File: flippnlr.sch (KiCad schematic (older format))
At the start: 87 parts, among them J1 Pwr In, J2 TP3, J3 TP1, J4 Opt Out, J5 Opt Out, J6 Data Out, J7 Data In, J8 TP2, U1 LD1117 3.3V, U10 TPL7407LA, U11 TPL7407LA, U12 TPL7407LA, U13 SN74HCS365, U2 SN74HCS594, U3 SN74HCS594, U4 SN74HCS594, U5 SN74HCS594, U6 SN74HCS594, U7 TPL7407LA, U8 TPL7407LA, U9 TPL7407LA

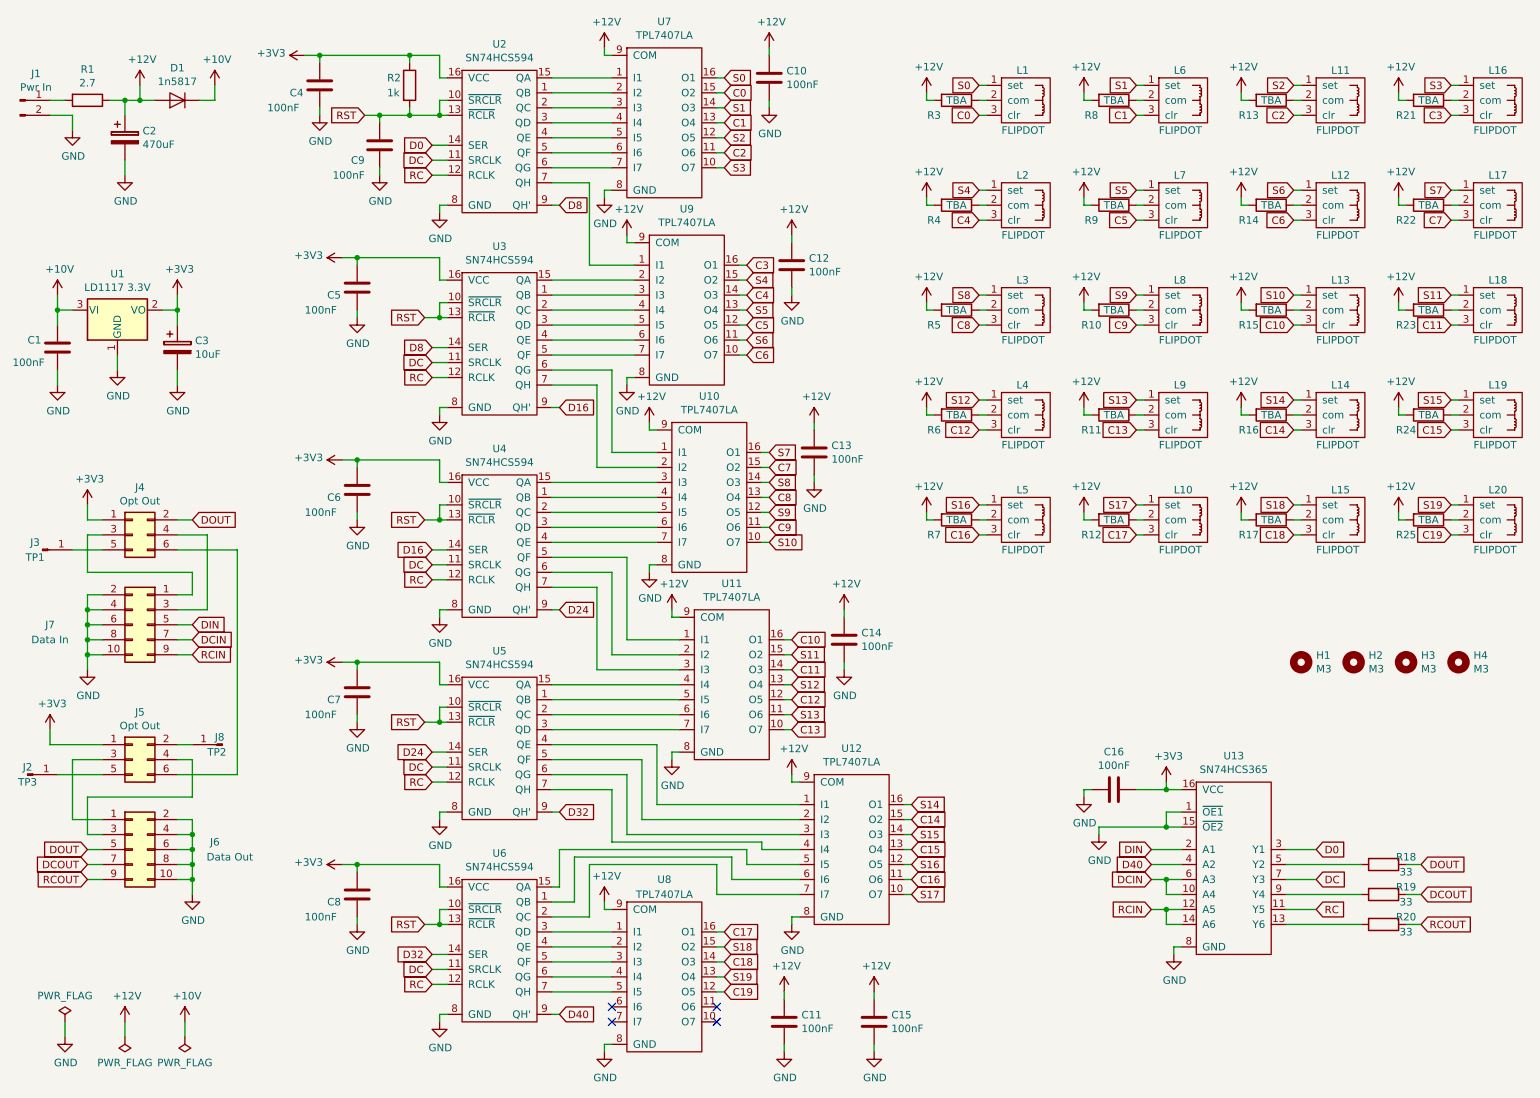
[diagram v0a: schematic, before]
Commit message: fix kicad lib path and begin layout
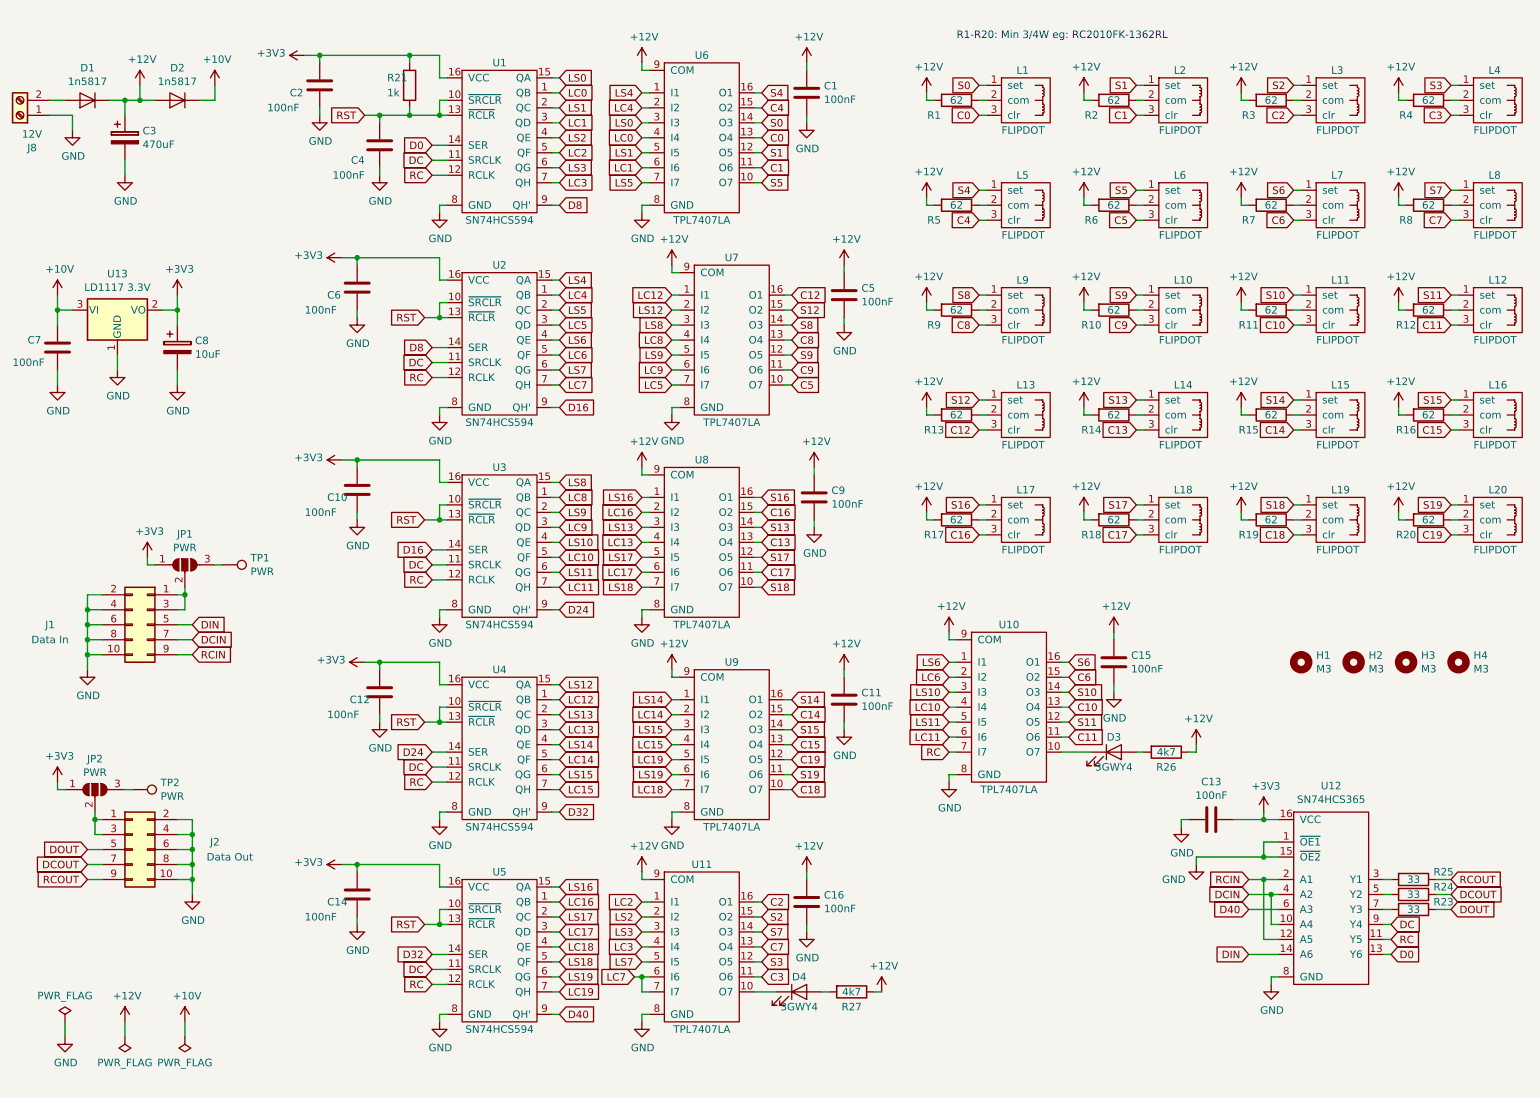
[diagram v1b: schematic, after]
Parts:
- removed J1: Pwr In, Connector_PinHeader_2.54mm:PinHeader_2x01_P2.54mm_Vertical, symbol Connector:Conn_01x02_Male
- removed J2: TP3, Connector_PinHeader_2.54mm:PinHeader_1x01_P2.54mm_Vertical, symbol Connector:Conn_01x01_Male
- removed J3: TP1, Connector_PinHeader_2.54mm:PinHeader_1x01_P2.54mm_Vertical, symbol Connector:Conn_01x01_Male
- removed J4, J5: Opt Out, Connector_PinHeader_2.54mm:PinHeader_2x03_P2.54mm_Vertical, symbol Connector_Generic:Conn_02x03_Odd_Even
- removed J8: TP2, Connector_PinHeader_2.54mm:PinHeader_1x01_P2.54mm_Vertical, symbol Connector:Conn_01x01_Male
- removed R1: 2.7, Resistor_THT:R_Axial_DIN0309_L9.0mm_D3.2mm_P12.70mm_Horizontal, symbol Device:R
- added D1: 1n5817, Diode_THT:D_A-405_P10.16mm_Horizontal, symbol Device:D
- added D3, D4: 3GWY4, LED_THT:LED_D3.0mm, symbol Device:LED
- added J8: 12V, TerminalBlock_Phoenix:TerminalBlock_Phoenix_PT-1,5-2-5.0-H_1x02_P5.00mm_Horizontal, symbol Connector:Screw_Terminal_01x02
- added JP1, JP2: PWR, Jumper:SolderJumper-3_P1.3mm_Open_RoundedPad1.0x1.5mm, symbol Jumper:SolderJumper_3_Open
- added R26, R27: 4k7, Resistor_SMD:R_0805_2012Metric_Pad1.15x1.40mm_HandSolder, symbol Device:R
- added TP1, TP2: PWR, TestPoint:TestPoint_Pad_D2.0mm, symbol Connector:TestPoint
- L1, L20: footprint Connector_PinHeader_2.54mm:PinHeader_1x03_P2.54mm_Vertical -> flipdot:Flipdot
- L10: renamed from L8; footprint Connector_PinHeader_2.54mm:PinHeader_1x03_P2.54mm_Vertical -> flipdot:Flipdot
- L11: renamed from L13; footprint Connector_PinHeader_2.54mm:PinHeader_1x03_P2.54mm_Vertical -> flipdot:Flipdot
- L12: renamed from L18; footprint Connector_PinHeader_2.54mm:PinHeader_1x03_P2.54mm_Vertical -> flipdot:Flipdot
- L13: renamed from L4; footprint Connector_PinHeader_2.54mm:PinHeader_1x03_P2.54mm_Vertical -> flipdot:Flipdot
- L14: renamed from L9; footprint Connector_PinHeader_2.54mm:PinHeader_1x03_P2.54mm_Vertical -> flipdot:Flipdot
- L15: renamed from L14; footprint Connector_PinHeader_2.54mm:PinHeader_1x03_P2.54mm_Vertical -> flipdot:Flipdot
- L16: renamed from L19; footprint Connector_PinHeader_2.54mm:PinHeader_1x03_P2.54mm_Vertical -> flipdot:Flipdot
- L17: renamed from L5; footprint Connector_PinHeader_2.54mm:PinHeader_1x03_P2.54mm_Vertical -> flipdot:Flipdot
- L18: renamed from L10; footprint Connector_PinHeader_2.54mm:PinHeader_1x03_P2.54mm_Vertical -> flipdot:Flipdot
- L19: renamed from L15; footprint Connector_PinHeader_2.54mm:PinHeader_1x03_P2.54mm_Vertical -> flipdot:Flipdot
- L2: renamed from L6; footprint Connector_PinHeader_2.54mm:PinHeader_1x03_P2.54mm_Vertical -> flipdot:Flipdot
- L3: renamed from L11; footprint Connector_PinHeader_2.54mm:PinHeader_1x03_P2.54mm_Vertical -> flipdot:Flipdot
- L4: renamed from L16; footprint Connector_PinHeader_2.54mm:PinHeader_1x03_P2.54mm_Vertical -> flipdot:Flipdot
- L5: renamed from L2; footprint Connector_PinHeader_2.54mm:PinHeader_1x03_P2.54mm_Vertical -> flipdot:Flipdot
- L6: renamed from L7; footprint Connector_PinHeader_2.54mm:PinHeader_1x03_P2.54mm_Vertical -> flipdot:Flipdot
- L7: renamed from L12; footprint Connector_PinHeader_2.54mm:PinHeader_1x03_P2.54mm_Vertical -> flipdot:Flipdot
- L8: renamed from L17; footprint Connector_PinHeader_2.54mm:PinHeader_1x03_P2.54mm_Vertical -> flipdot:Flipdot
- L9: renamed from L3; footprint Connector_PinHeader_2.54mm:PinHeader_1x03_P2.54mm_Vertical -> flipdot:Flipdot
- R1: renamed from R3; value TBA -> 62; footprint Resistor_SMD:R_1210_3225Metric_Pad1.42x2.65mm_HandSolder -> Resistor_SMD:R_2010_5025Metric_Pad1.52x2.65mm_HandSolder
- R10: value TBA -> 62; footprint Resistor_SMD:R_1210_3225Metric_Pad1.42x2.65mm_HandSolder -> Resistor_SMD:R_2010_5025Metric_Pad1.52x2.65mm_HandSolder
- R11: renamed from R15; value TBA -> 62; footprint Resistor_SMD:R_1210_3225Metric_Pad1.42x2.65mm_HandSolder -> Resistor_SMD:R_2010_5025Metric_Pad1.52x2.65mm_HandSolder
- R12: renamed from R23; value TBA -> 62; footprint Resistor_SMD:R_1210_3225Metric_Pad1.42x2.65mm_HandSolder -> Resistor_SMD:R_2010_5025Metric_Pad1.52x2.65mm_HandSolder
- R13: renamed from R6; value TBA -> 62; footprint Resistor_SMD:R_1210_3225Metric_Pad1.42x2.65mm_HandSolder -> Resistor_SMD:R_2010_5025Metric_Pad1.52x2.65mm_HandSolder
- R14: renamed from R11; value TBA -> 62; footprint Resistor_SMD:R_1210_3225Metric_Pad1.42x2.65mm_HandSolder -> Resistor_SMD:R_2010_5025Metric_Pad1.52x2.65mm_HandSolder
- R15: renamed from R16; value TBA -> 62; footprint Resistor_SMD:R_1210_3225Metric_Pad1.42x2.65mm_HandSolder -> Resistor_SMD:R_2010_5025Metric_Pad1.52x2.65mm_HandSolder
- R16: renamed from R24; value TBA -> 62; footprint Resistor_SMD:R_1210_3225Metric_Pad1.42x2.65mm_HandSolder -> Resistor_SMD:R_2010_5025Metric_Pad1.52x2.65mm_HandSolder
- R17: renamed from R7; value TBA -> 62; footprint Resistor_SMD:R_1210_3225Metric_Pad1.42x2.65mm_HandSolder -> Resistor_SMD:R_2010_5025Metric_Pad1.52x2.65mm_HandSolder
- R18: renamed from R12; value TBA -> 62; footprint Resistor_SMD:R_1210_3225Metric_Pad1.42x2.65mm_HandSolder -> Resistor_SMD:R_2010_5025Metric_Pad1.52x2.65mm_HandSolder
- R19: renamed from R17; value TBA -> 62; footprint Resistor_SMD:R_1210_3225Metric_Pad1.42x2.65mm_HandSolder -> Resistor_SMD:R_2010_5025Metric_Pad1.52x2.65mm_HandSolder
- R2: renamed from R8; value TBA -> 62; footprint Resistor_SMD:R_1210_3225Metric_Pad1.42x2.65mm_HandSolder -> Resistor_SMD:R_2010_5025Metric_Pad1.52x2.65mm_HandSolder
- R20: renamed from R25; value TBA -> 62; footprint Resistor_SMD:R_1210_3225Metric_Pad1.42x2.65mm_HandSolder -> Resistor_SMD:R_2010_5025Metric_Pad1.52x2.65mm_HandSolder
- R3: renamed from R13; value TBA -> 62; footprint Resistor_SMD:R_1210_3225Metric_Pad1.42x2.65mm_HandSolder -> Resistor_SMD:R_2010_5025Metric_Pad1.52x2.65mm_HandSolder
- R4: renamed from R21; value TBA -> 62; footprint Resistor_SMD:R_1210_3225Metric_Pad1.42x2.65mm_HandSolder -> Resistor_SMD:R_2010_5025Metric_Pad1.52x2.65mm_HandSolder
- R5: renamed from R4; value TBA -> 62; footprint Resistor_SMD:R_1210_3225Metric_Pad1.42x2.65mm_HandSolder -> Resistor_SMD:R_2010_5025Metric_Pad1.52x2.65mm_HandSolder
- R6: renamed from R9; value TBA -> 62; footprint Resistor_SMD:R_1210_3225Metric_Pad1.42x2.65mm_HandSolder -> Resistor_SMD:R_2010_5025Metric_Pad1.52x2.65mm_HandSolder
- R7: renamed from R14; value TBA -> 62; footprint Resistor_SMD:R_1210_3225Metric_Pad1.42x2.65mm_HandSolder -> Resistor_SMD:R_2010_5025Metric_Pad1.52x2.65mm_HandSolder
- R8: renamed from R22; value TBA -> 62; footprint Resistor_SMD:R_1210_3225Metric_Pad1.42x2.65mm_HandSolder -> Resistor_SMD:R_2010_5025Metric_Pad1.52x2.65mm_HandSolder
- R9: renamed from R5; value TBA -> 62; footprint Resistor_SMD:R_1210_3225Metric_Pad1.42x2.65mm_HandSolder -> Resistor_SMD:R_2010_5025Metric_Pad1.52x2.65mm_HandSolder
- renumbered C10 to C1, C6 to C10, C14 to C11, C7 to C12, C16 to C13, C8 to C14, C11 to C15, C15 to C16, C4 to C2, C2 to C3, C9 to C4, C12 to C5, C5 to C6, C1 to C7, C3 to C8, C13 to C9, D1 to D2, J7 to J1, J6 to J2, R2 to R21, R18 to R23, R19 to R24, R20 to R25, U2 to U1, U12 to U10, U8 to U11, U13 to U12, U1 to U13, U3 to U2, U4 to U3, U5 to U4, U6 to U5, U7 to U6, U9 to U7, U10 to U8, U11 to U9
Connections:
- net +12V: now also D1.1 (K), R26.1, R27.1
- net +3V3: now also JP1.1 (A), JP2.1 (A)
- net C0: now also U6.13 (O4); no longer U6.15 (O2)
- net C1: now also U6.11 (O6); no longer U6.13 (O4)
- net C10: now also U10.13 (O4); no longer U9.16 (O1)
- net C11: now also U10.11 (O6); no longer U9.14 (O3)
- net C12: now also U7.16 (O1); no longer U9.12 (O5)
- net C13: now also U8.13 (O4); no longer U9.10 (O7)
- net C14: now also U9.15 (O2); no longer U10.15 (O2)
- net C15: now also U9.13 (O4); no longer U10.13 (O4)
- net C16: now also U8.15 (O2); no longer U10.11 (O6)
- net C17: now also U8.11 (O6); no longer U11.16 (O1)
- net C18: now also U9.10 (O7); no longer U11.14 (O3)
- net C19: now also U9.12 (O5); no longer U11.12 (O5)
- net C2: now also U11.16 (O1); no longer U6.11 (O6)
- net C3: now also U11.11 (O6); no longer U7.16 (O1)
- net C4: now also U6.15 (O2); no longer U7.14 (O3)
- net C5: now also U7.10 (O7); no longer U7.12 (O5)
- net C6: now also U10.15 (O2); no longer U7.10 (O7)
- net C7: now also U11.13 (O4); no longer U8.15 (O2)
- net C8: now also U7.13 (O4); no longer U8.13 (O4)
- net C9: now also U7.11 (O6); no longer U8.11 (O6)
- net D0: now also U12.13 (Y6); no longer U12.3 (Y1)
- net D40: now also U12.6 (A3); no longer U12.4 (A2)
- net DC: now also U12.9 (Y4); no longer U12.7 (Y3)
- net DCIN: now also U12.4 (A2); no longer U12.6 (A3)
- net DIN: now also U12.14 (A6); no longer U12.2 (A1)
- net GND: now also J8.1 (Pin_1)
- net RC: now also U10.7 (I7)
- net RCIN: now also U12.2 (A1); no longer U12.14 (A6)
- net S0: now also U6.14 (O3); no longer U6.16 (O1)
- net S1: now also U6.12 (O5); no longer U6.14 (O3)
- net S10: now also U10.14 (O3); no longer U8.10 (O7)
- net S11: now also U10.12 (O5); no longer U9.15 (O2)
- net S12: now also U7.15 (O2); no longer U9.13 (O4)
- net S13: now also U8.14 (O3); no longer U9.11 (O6)
- net S14: now also U9.16 (O1); no longer U10.16 (O1)
- net S15: now also U9.14 (O3); no longer U10.14 (O3)
- net S16: now also U8.16 (O1); no longer U10.12 (O5)
- net S17: now also U8.12 (O5); no longer U10.10 (O7)
- net S18: now also U8.10 (O7); no longer U11.15 (O2)
- net S19: now also U9.11 (O6); no longer U11.13 (O4)
- net S2: now also U11.15 (O2); no longer U6.12 (O5)
- net S3: now also U11.12 (O5); no longer U6.10 (O7)
- net S4: now also U6.16 (O1); no longer U7.15 (O2)
- net S5: now also U6.10 (O7); no longer U7.13 (O4)
- net S6: now also U10.16 (O1); no longer U7.11 (O6)
- net S7: now also U11.14 (O3); no longer U8.16 (O1)
- net S8: now also U7.14 (O3); no longer U8.14 (O3)
- net S9: now also U7.12 (O5); no longer U8.12 (O5)
- net at J1.1 (Pin_1): now also J1.3 (Pin_3), JP1.2 (C)
- net at J2.1 (Pin_1): now also J2.3 (Pin_3), JP2.2 (C)
- net at R25.2: now also U12.3 (Y1); no longer U12.13 (Y6)
- net at R24.2: now also U12.5 (Y2); no longer U12.9 (Y4)
- net at R23.2: now also U12.7 (Y3); no longer U12.5 (Y2)
- net LC17: now reaches U5.3 (QD)
- net LC17: now also U8.6 (I6); no longer U11.1 (I1)
- net at U11.10 (O7): now also D4.1 (K)
- net LC18: now reaches U5.4 (QE)
- net LC18: now also U9.7 (I7); no longer U11.2 (I2)
- net LS18: now reaches U5.5 (QF)
- net LS18: now also U8.7 (I7); no longer U11.3 (I3)
- net LC3: now reaches U11.4 (I4)
- net LC3: now also U1.7 (QH); no longer U5.6 (QG)
- net LC19: now reaches U5.7 (QH)
- net LC19: now also U9.5 (I5); no longer U11.5 (I5)
- net LC7: now reaches U11.6 (I6)
- net LC7: now also U11.7 (I7), U2.7 (QH)
- net LC0: now reaches U1.1 (QB)
- net LC0: now also U6.4 (I4); no longer U6.2 (I2)
- net LS0: now reaches U1.15 (QA)
- net LS0: now also U6.3 (I3); no longer U6.1 (I1)
- net LS1: now reaches U1.2 (QC)
- net LS1: now also U6.5 (I5); no longer U6.3 (I3)
- net LC1: now reaches U1.3 (QD)
- net LC1: now also U6.6 (I6); no longer U6.4 (I4)
- net LS2: now reaches U1.4 (QE)
- net LS2: now also U11.2 (I2); no longer U6.5 (I5)
- net LC2: now reaches U1.5 (QF)
- net LC2: now also U11.1 (I1); no longer U6.6 (I6)
- net LS3: now reaches U1.6 (QG)
- net LS3: now also U11.3 (I3); no longer U6.7 (I7)
- net LC12: now reaches U7.1 (I1)
- net LC12: now also U4.1 (QB); no longer U1.7 (QH)
- net LC10: now reaches U3.5 (QF)
- net LC10: now also U10.4 (I4); no longer U9.1 (I1)
- net LC14: now reaches U9.2 (I2)
- net LC14: now also U4.5 (QF); no longer U3.6 (QG)
- net LC11: now reaches U3.7 (QH)
- net LC11: now also U10.6 (I6); no longer U9.3 (I3)
- net LC15: now reaches U9.4 (I4)
- net LC15: now also U4.7 (QH); no longer U4.15 (QA)
- net LS13: now reaches U4.2 (QC)
- net LS13: now also U8.3 (I3); no longer U9.6 (I6)
- net LC13: now reaches U4.3 (QD)
- net LC13: now also U8.4 (I4); no longer U9.7 (I7)
- net LC4: now reaches U2.1 (QB)
- net LC4: now also U6.2 (I2); no longer U7.3 (I3)
- net LS12: now reaches U7.2 (I2)
- net LS12: now also U4.15 (QA); no longer U2.15 (QA)
- net LC8: now reaches U7.4 (I4)
- net LC8: now also U3.1 (QB); no longer U2.2 (QC)
- net LC5: now reaches U2.3 (QD)
- net LC5: now also U7.7 (I7); no longer U7.5 (I5)
- net LC9: now reaches U7.6 (I6)
- net LC9: now also U3.3 (QD); no longer U2.4 (QE)
- net LC6: now reaches U2.5 (QF)
- net LC6: now also U10.2 (I2); no longer U7.7 (I7)
- net LS16: now reaches U8.1 (I1)
- net LS16: now also U5.15 (QA); no longer U2.6 (QG)
- net LC16: now reaches U8.2 (I2)
- net LC16: now also U5.1 (QB); no longer U2.7 (QH)
- net LS14: now reaches U4.4 (QE)
- net LS14: now also U9.1 (I1); no longer U10.1 (I1)
- net LS10: now reaches U10.3 (I3)
- net LS10: now also U3.4 (QE); no longer U4.6 (QG)
- net LS11: now reaches U10.5 (I5)
- net LS11: now also U3.6 (QG); no longer U5.15 (QA)
- net LS17: now reaches U5.2 (QC)
- net LS17: now also U8.5 (I5); no longer U10.7 (I7)
- net LS8: now reaches U3.15 (QA)
- net LS8: now also U7.3 (I3); no longer U8.3 (I3)
- net LS9: now reaches U3.2 (QC)
- net LS9: now also U7.5 (I5); no longer U8.5 (I5)
- new net: D3.1 (K), U10.10 (O7)
- new net: D3.2 (A), R26.2
- new net: D4.2 (A), R27.2
- new net: JP1.3 (B), TP1.1
- new net: JP2.3 (B), TP2.1
- new net: D1.2 (A), J8.2 (Pin_2)
- new net LS15: U4.6 (QG), U9.3 (I3)
- new net LS19: U5.6 (QG), U9.6 (I6)
- new net LS4: U2.15 (QA), U6.1 (I1)
- new net LS5: U2.2 (QC), U6.7 (I7)
- new net LS6: U10.1 (I1), U2.4 (QE)
- new net LS7: U11.5 (I5), U2.6 (QG)
- no-connect marks 4 -> 0
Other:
- note added: "R1-R20: Min 3/4W eg: RC2010FK-1362RL"
- moved on the sheet: C1, C11, C12, C13, C15, C16, C5, C9, R23, R24, R25, U10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

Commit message: reroute signals slightly
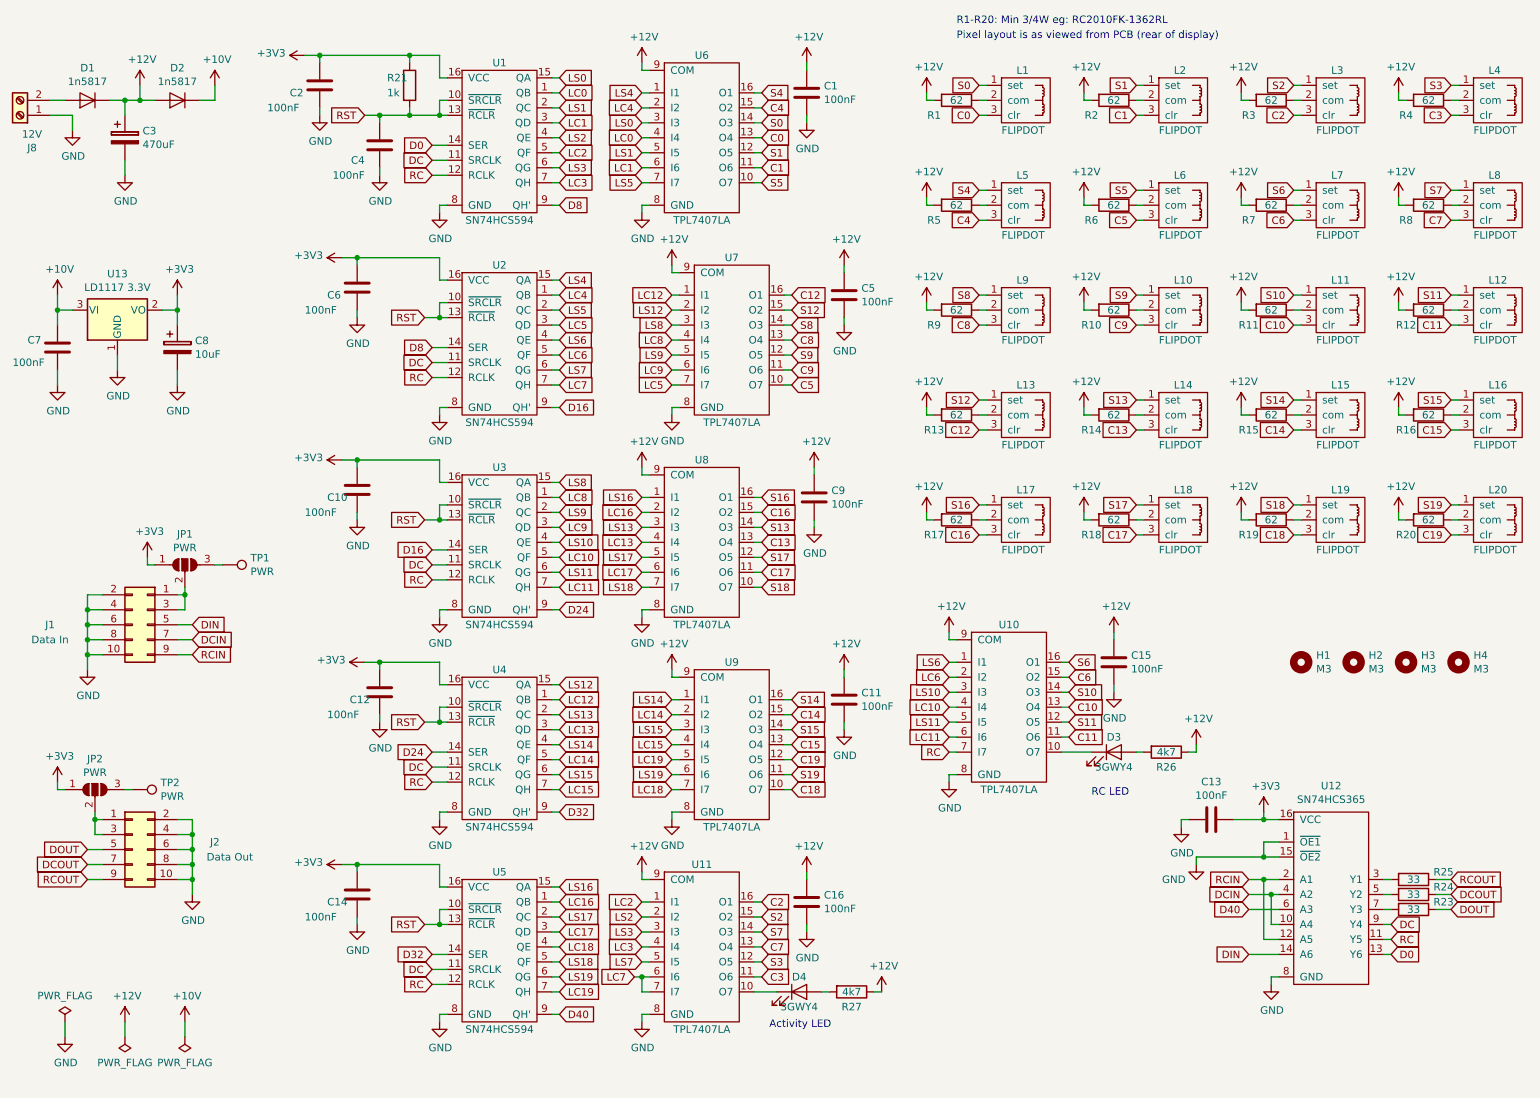
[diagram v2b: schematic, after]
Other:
- note added: "Activity LED"
- note added: "Pixel layout is as viewed from PCB (rear of display)"
- note added: "RC LED"
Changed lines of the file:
@@
 Wire Wire Line
 	10000 3950 10050 3950
-Text Notes 7050 750  0    50   ~ 0
+Text Notes 7050 650  0    50   ~ 0
 R1-R20: Min 3/4W eg: RC2010FK-1362RL
 Wire Wire Line
@@
 Wire Wire Line
 	4950 7000 5000 7000
+Text Notes 7950 5800 0    50   ~ 0
+RC LED
+Text Notes 5800 7350 0    50   ~ 0
+Activity LED
+Text Notes 7050 750  0    50   ~ 0
+Pixel layout is as viewed from PCB (rear of display)
 $EndSCHEMATC

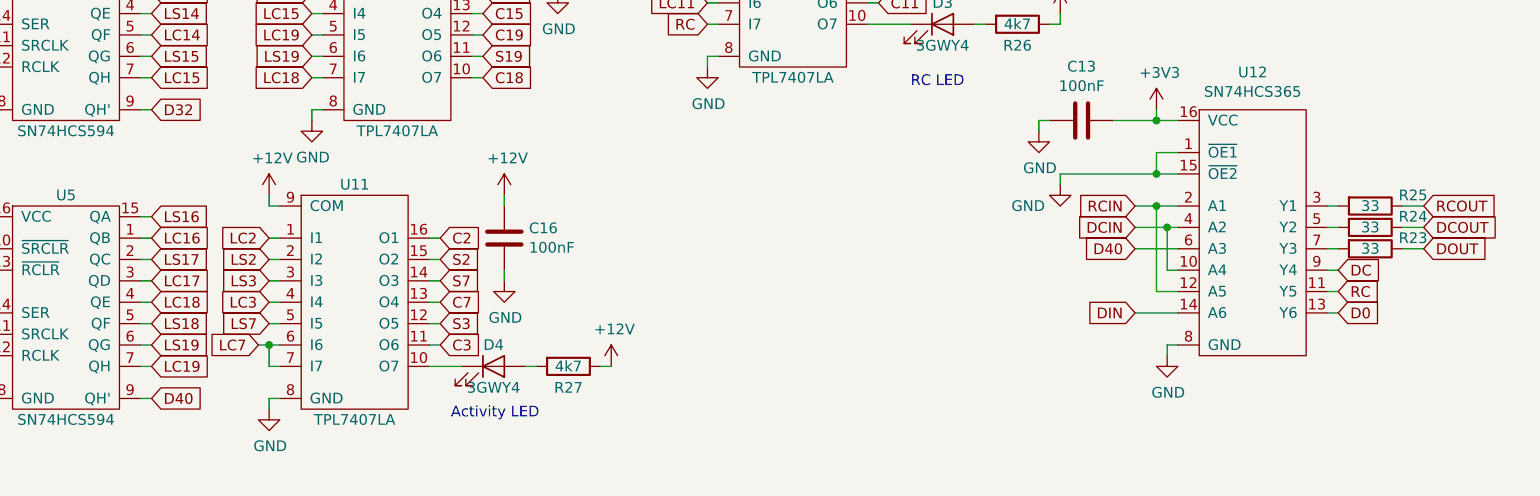
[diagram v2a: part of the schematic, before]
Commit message: correct mis-wired U5
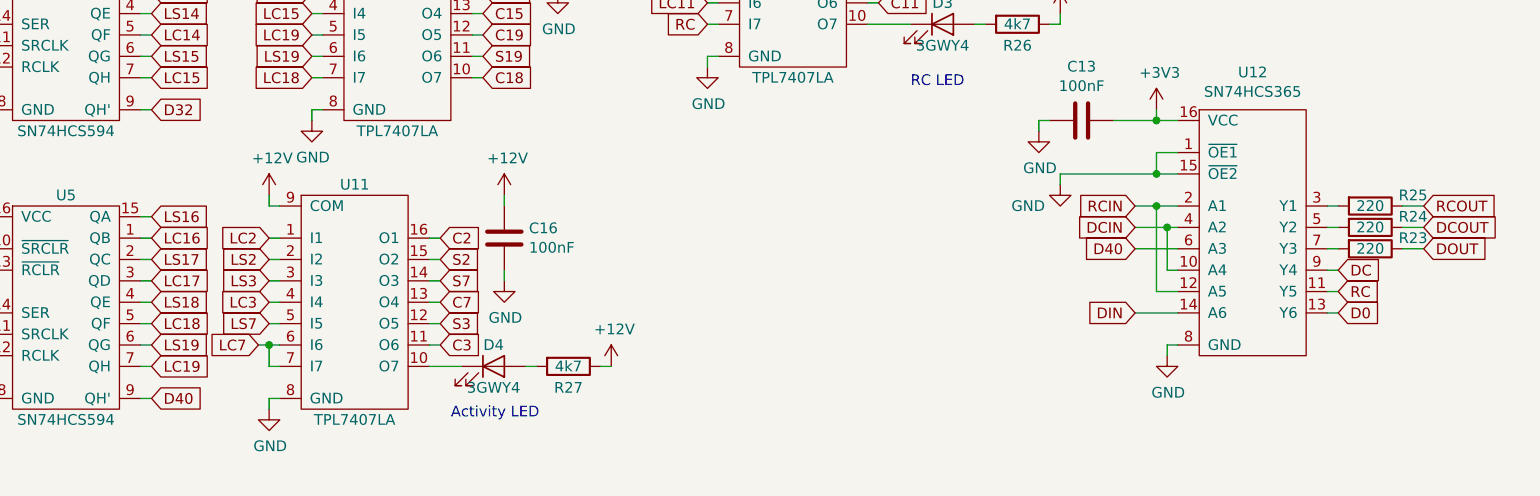
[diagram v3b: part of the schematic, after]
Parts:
- R23, R24, R25: value 33 -> 220
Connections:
- net LC18: now also U5.5 (QF); no longer U5.4 (QE)
- net LS18: now also U5.4 (QE); no longer U5.5 (QF)
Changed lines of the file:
@@
 encoding utf-8
 Sheet 1 1
-Title "Flip Panel R5x4"
+Title "Flip Panel R4x5"
 Date "2021-09-12"
 Rev "1.1"
@@
 P 10100 6350
 F 0 "R25" V 10050 6550 50  0000 C CNN
-F 1 "33" V 10100 6350 50  0000 C CNN
+F 1 "220" V 10100 6350 50  0000 C CNN
 F 2 "Resistor_SMD:R_0805_2012Metric_Pad1.15x1.40mm_HandSolder" V 10030 6350 50  0001 C CNN
 F 3 "~" H 10100 6350 50  0001 C CNN
@@
 P 10100 6450
 F 0 "R24" V 10050 6650 50  0000 C CNN
-F 1 "33" V 10100 6450 50  0000 C CNN
+F 1 "220" V 10100 6450 50  0000 C CNN
 F 2 "Resistor_SMD:R_0805_2012Metric_Pad1.15x1.40mm_HandSolder" V 10030 6450 50  0001 C CNN
 F 3 "~" H 10100 6450 50  0001 C CNN
@@
 P 10100 6550
 F 0 "R23" V 10050 6750 50  0000 C CNN
-F 1 "33" V 10100 6550 50  0000 C CNN
+F 1 "220" V 10100 6550 50  0000 C CNN
 F 2 "Resistor_SMD:R_0805_2012Metric_Pad1.15x1.40mm_HandSolder" V 10030 6550 50  0001 C CNN
 F 3 "~" H 10100 6550 50  0001 C CNN
@@
 Text GLabel 4400 6700 2    50   Input ~ 0
 LC17
-Text GLabel 4400 6800 2    50   Input ~ 0
-LC18
 Text GLabel 4400 6900 2    50   Input ~ 0
+LC18
+Text GLabel 4400 6800 2    50   Input ~ 0
 LS18
 Text GLabel 4400 7000 2    50   Input ~ 0
